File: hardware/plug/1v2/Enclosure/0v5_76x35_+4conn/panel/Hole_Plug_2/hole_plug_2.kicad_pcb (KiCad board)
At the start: 2 copper layers, 12.2 x 4.6 mm, 4 parts

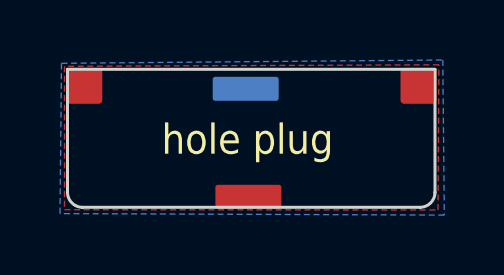
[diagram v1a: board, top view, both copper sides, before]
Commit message: add 3d models in .wrl
used @2ftg .step models and imported them into FreeCAD
added .wrl for Rear panels and hole plugs
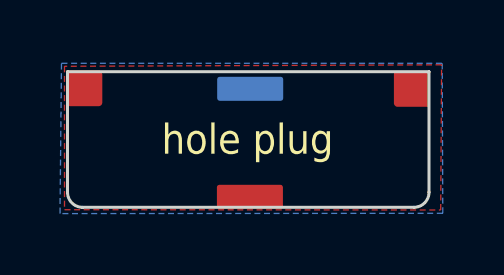
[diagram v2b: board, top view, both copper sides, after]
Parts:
- moved REF** 0.24 mm to (69.0, 120.1)
- moved REF** 0.15 mm to (63.6, 120.1)
- moved REF** 0.08 mm to (58.1, 120.1)
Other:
- board size 12.2 x 4.6 mm -> 12 x 4.5 mm
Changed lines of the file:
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@@
     (links 3)
     (no_connects 1)
-    (area 55.672143 114.8775 71.647857 126.127857)
+    (area 55.672143 114.8775 71.747857 126.127857)
     (thickness 1.6)
     (drawings 27)
@@
     (38 B.Mask user)
     (39 F.Mask user)
-    (40 Dwgs.User user)
+    (40 Dwgs.User user hide)
     (41 Cmts.User user)
     (42 Eco1.User user)
@@
     (pad_to_mask_clearance 0)
     (aux_axis_origin 57.27 119.21)
-    (grid_origin 57.27 119.21)
+    (grid_origin 58.03 124.06)
     (visible_elements 7FFFFFFF)
     (pcbplotparams
@@
   )
   (module Connect:1pin (layer B.Cu)
-    (at 63.47 120.11 90)
+    (at 63.62 120.11 90)
     (descr "module 1 pin (ou trou mecanique de percage)")
     (tags DEV)
@@
   )
   (module Connect:1pin (layer F.Cu)
-    (at 58.09 120.01)
+    (at 58.09 120.09)
     (descr "module 1 pin (ou trou mecanique de percage)")
     (tags DEV)
@@
   )
   (module Connect:1pin (layer F.Cu)
-    (at 69.23 120.01)
+    (at 69.01 120.11)
     (descr "module 1 pin (ou trou mecanique de percage)")
     (tags DEV)
@@
   )
   (module Connect:1pin (layer F.Cu)
-    (at 63.56 123.71 270)
+    (at 63.61 123.71 270)
     (descr "module 1 pin (ou trou mecanique de percage)")
     (tags DEV)
@@
     (effects (font (size 1 0.9) (thickness 0.2)))
   )
-  (gr_line (start 69.78 119.46) (end 69.78 123.56) (layer Edge.Cuts) (width 0.1))
-  (gr_line (start 57.53 119.46) (end 69.78 119.46) (layer Edge.Cuts) (width 0.1))
-  (gr_line (start 57.53 123.55) (end 57.53 119.46) (layer Edge.Cuts) (width 0.1))
-  (gr_line (start 69.28 124.06) (end 58.03 124.06) (layer Edge.Cuts) (width 0.1))
-  (gr_arc (start 69.28 123.56) (end 69.78 123.56) (angle 90) (layer Edge.Cuts) (width 0.1))
+  (gr_line (start 69.58 119.54) (end 69.58 123.56) (layer Edge.Cuts) (width 0.1))
+  (gr_line (start 57.53 119.54) (end 69.58 119.54) (layer Edge.Cuts) (width 0.1))
+  (gr_line (start 57.53 123.55) (end 57.53 119.54) (layer Edge.Cuts) (width 0.1))
+  (gr_line (start 69.08 124.06) (end 58.03 124.06) (layer Edge.Cuts) (width 0.1))
+  (gr_arc (start 69.08 123.56) (end 69.58 123.56) (angle 90) (layer Edge.Cuts) (width 0.1))
   (gr_arc (start 58.03 123.56) (end 58.03 124.06) (angle 90) (layer Edge.Cuts) (width 0.1))
   (gr_line (start 69.913521 119.199078) (end 57.413521 119.199078) (layer Dwgs.User) (width 0.1))
@@
     (polygon
       (pts
-        (xy 57.43 124.14) (xy 69.88 124.15) (xy 69.91 119.31) (xy 57.43 119.36)
+        (xy 57.43 124.14) (xy 69.97 124.15) (xy 70 119.31) (xy 57.43 119.36)
       )
     )
@@
     (polygon
       (pts
-        (xy 57.33 119.26) (xy 70.04 119.15) (xy 70.09 124.32) (xy 57.28 124.27)
+        (xy 57.33 119.26) (xy 70.02 119.26) (xy 70.04 124.26) (xy 57.28 124.27)
       )
     )
